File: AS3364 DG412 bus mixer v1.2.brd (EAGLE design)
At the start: 82.6 x 36.8 mm, 123 parts, among them IC1 PCA9539PW, IC10 DG412-J, IC11 DG412-J, IC2 TL074JT, IC3 TL072JT, IC4 TL074JT, IC5 TL072JT, IC6 TL072JT, IC8 DG412-J, IC9 DG412-J

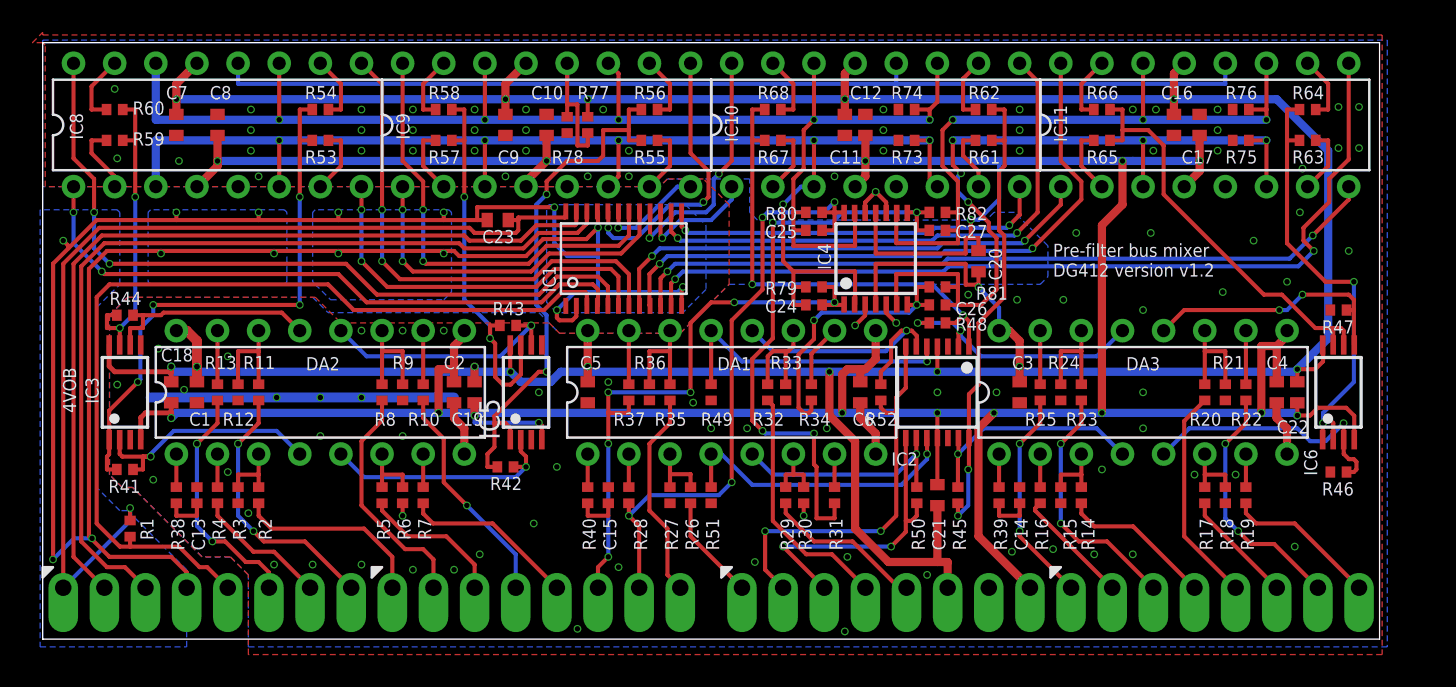
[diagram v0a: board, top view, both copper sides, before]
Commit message: Moved corner to origo
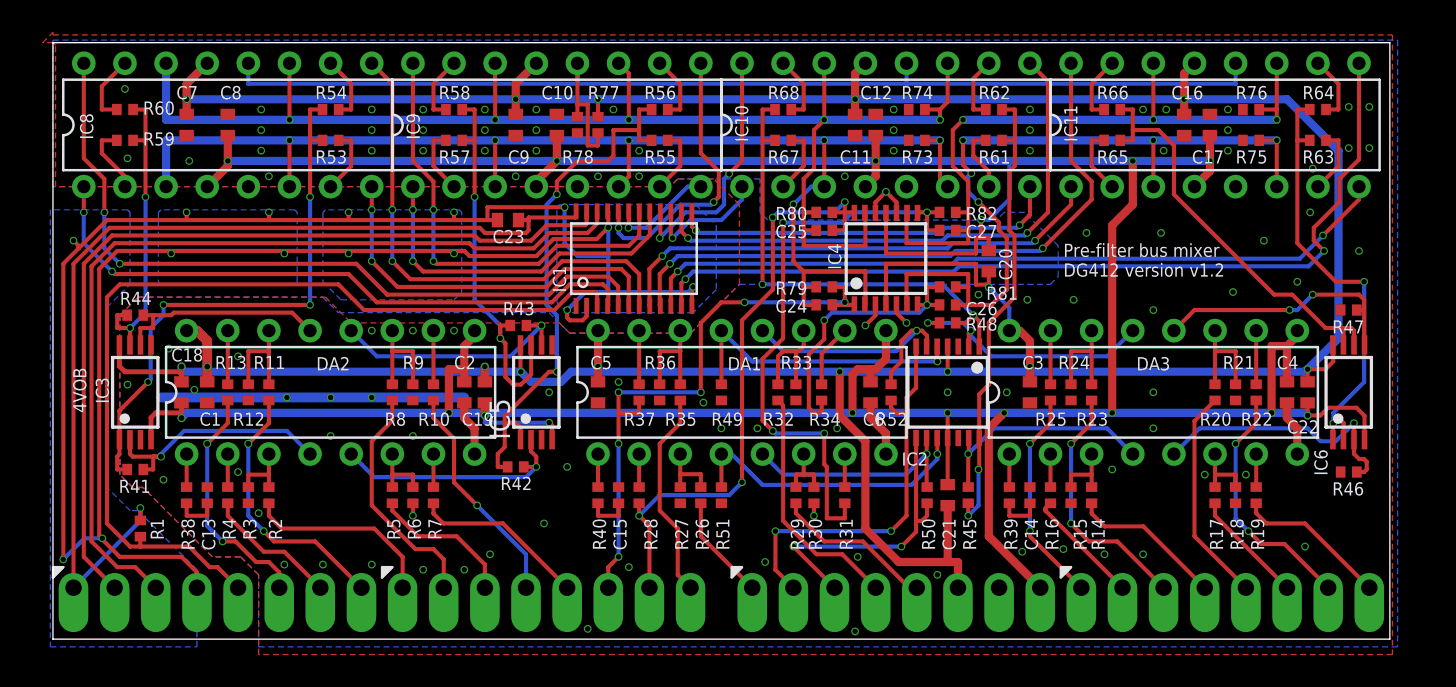
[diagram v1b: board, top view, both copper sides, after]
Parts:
- moved C14 0.64 mm to (60.3, 8.89)
- moved C17 0.64 mm to (71.4, 31.8)
- moved C22 0.64 mm to (77.5, 15.2)
- moved C3 0.64 mm to (60.3, 15.2)
- moved C4 0.64 mm to (76.2, 15.2)
- moved C6 0.64 mm to (50.5, 15.2)
- moved DA1 0.64 mm to (42.5, 15.2)
- moved IC10 0.64 mm to (51.4, 31.8)
- moved IC4 0.64 mm to (51.4, 23.5)
- moved IC6 0.64 mm to (80.0, 15.2)
- moved R14 0.64 mm to (64.1, 8.89)
- moved R15 0.64 mm to (62.9, 8.89)
- moved R18 0.64 mm to (73.0, 8.89)
- moved R19 0.64 mm to (74.3, 8.89)
- moved R21 0.64 mm to (73.0, 15.2)
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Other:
- board size 82.6 x 36.8 mm -> 82.5 x 36.8 mm

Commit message: Updated pin spacing to 2.54mm to still fit breadboard
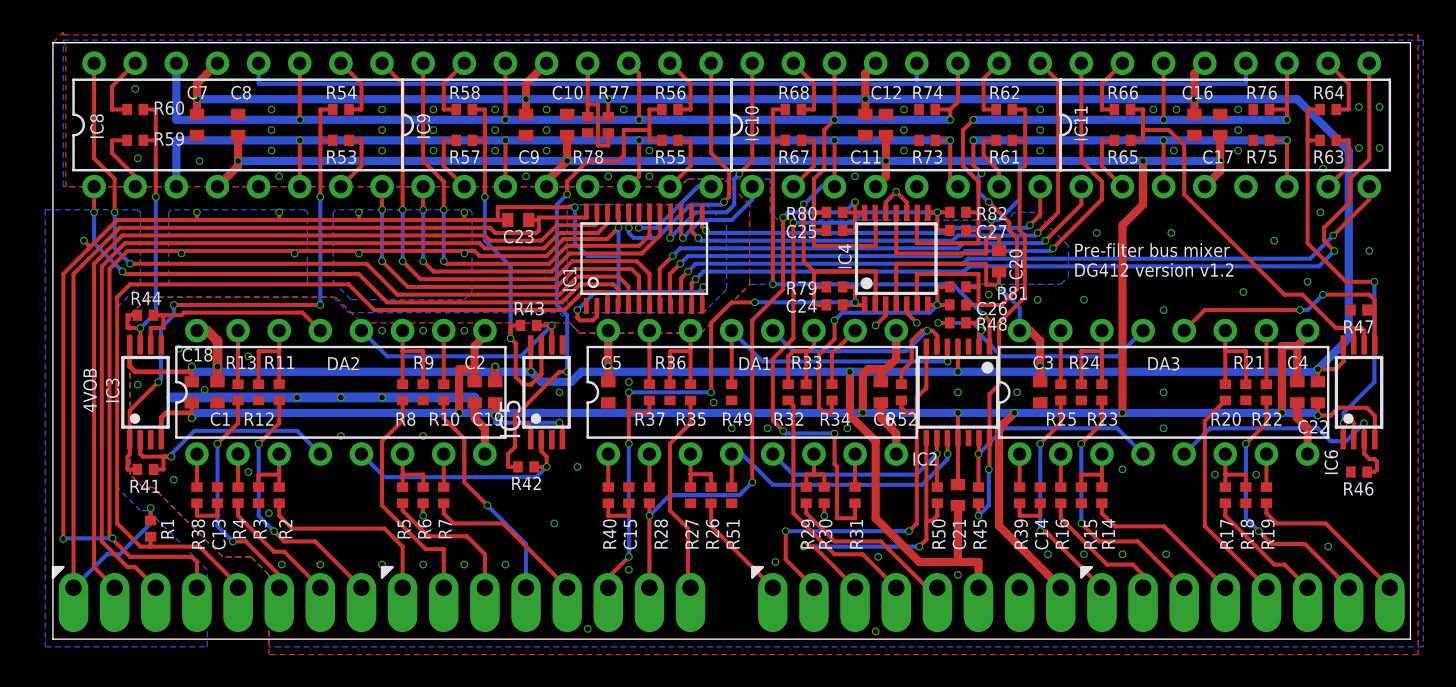
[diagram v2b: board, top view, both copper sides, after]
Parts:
- moved SV4 1.27 mm to (53.3, 3.17)
- moved SV3 1.27 mm to (73.7, 3.17)
- moved C12 0.64 mm to (51.4, 31.8)
- moved C15 0.64 mm to (35.6, 8.89)
- moved C16 0.64 mm to (70.5, 31.8)
- moved C17 0.64 mm to (72.1, 31.8)
- moved C20 0.64 mm to (58.4, 23.3)
- moved C21 0.64 mm to (55.9, 8.89)
- moved C22 0.64 mm to (78.1, 15.2)
- moved C26 0.64 mm to (55.9, 21.7)
- moved C27 0.64 mm to (55.9, 25.2)
- moved DA3 0.64 mm to (68.6, 15.2)
- moved IC1 0.64 mm to (36.5, 23.5)
- moved IC11 0.64 mm to (72.4, 31.8)
- moved IC2 0.64 mm to (55.9, 15.2)
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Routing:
- net DGND: track 137.3 -> 136.2 mm
- net +3V3: track 61.3 -> 62.3 mm
- net IN6: track 7.32 -> 8.25 mm
- net OUT_B: track 18.9 -> 19.8 mm
- net IN1: track 14.9 -> 14.1 mm
- net IN7: track 15.3 -> 15.9 mm
- net CV6: track 9.52 -> 10.2 mm
- net CV1: track 16.5 -> 15.8 mm
- net IN4: track 10.8 -> 10.2 mm
- net IN2: track 8.33 -> 7.69 mm
- net CV5: track 15.5 -> 16.1 mm
- net IN8: track 9.50 -> 10.1 mm
- net CV_B_WET: track 9.98 -> 10.6 mm
- net CV8: track 7.06 -> 7.69 mm
- net SCL: track 55.5 -> 54.8 mm
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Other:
- board size 82.5 x 36.8 mm -> 83.8 x 36.8 mm
